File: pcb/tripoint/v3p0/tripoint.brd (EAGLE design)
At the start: 30.5 x 16.4 mm, 72 parts, among them J2 TC2030-JLINK-NL, T1 HHM1595A1, U1 STM32F091CC, U2 DW1000, U3 SKY13317, U4 LXDC2HN18A, X1 38.4M, X2 16M

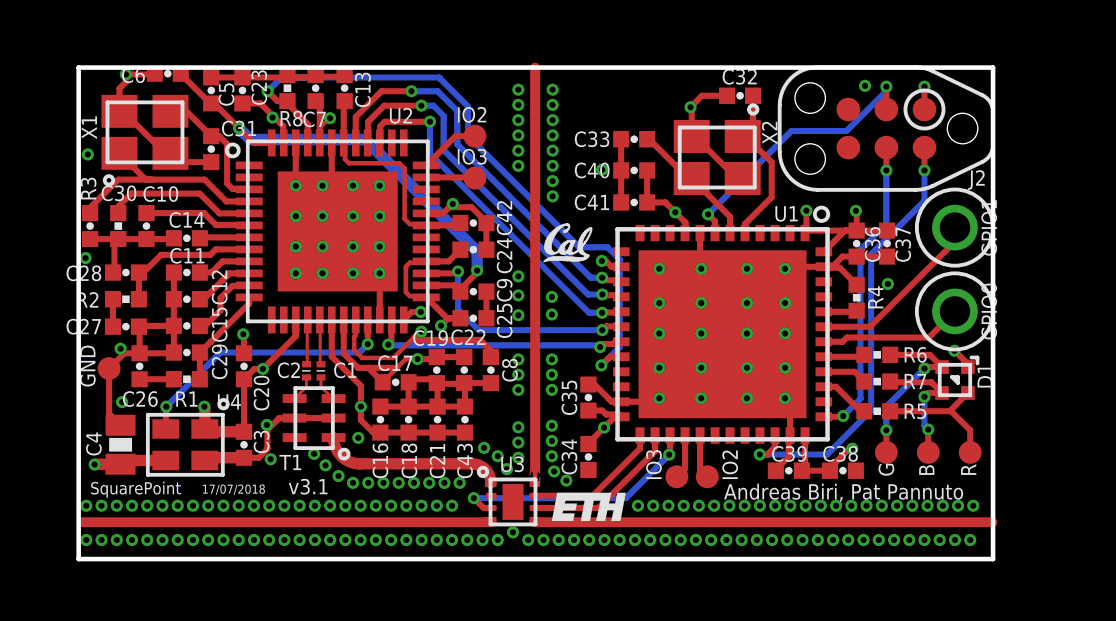
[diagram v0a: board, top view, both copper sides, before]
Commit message: fixed silk screen, increased space between 0201 capacitors
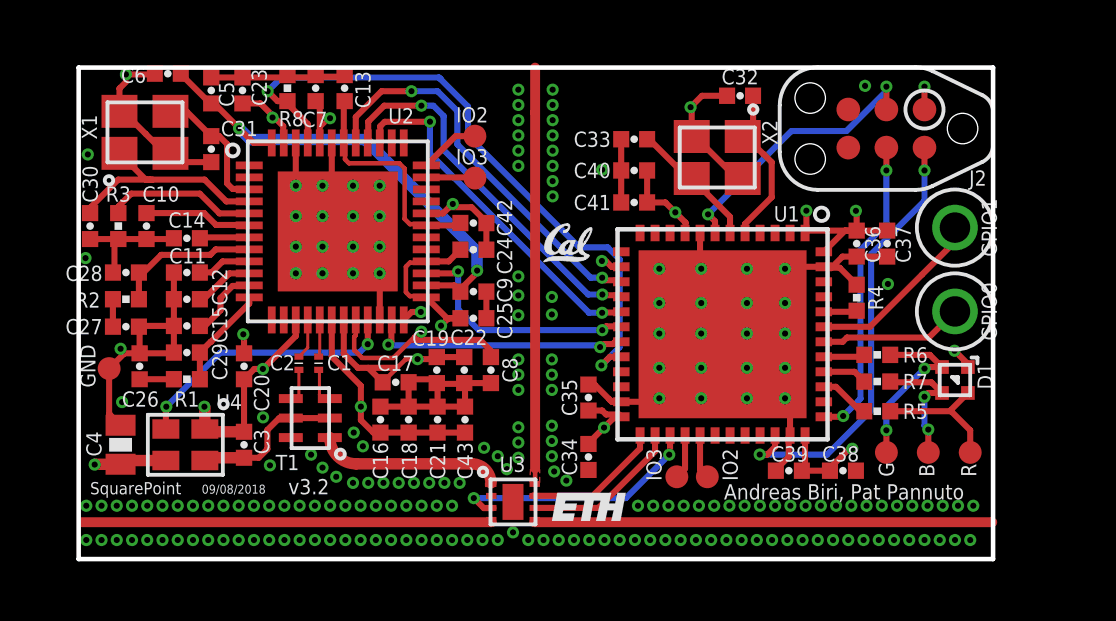
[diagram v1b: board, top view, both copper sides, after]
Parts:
- moved C2 0.36 mm to (-7.90, 0.69)
- moved C1 0.27 mm to (-7.24, 0.69)
- moved T1 0.13 mm to (-7.52, -1.14)
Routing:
- net GND: track 84.2 -> 84.1 mm, vias 204 -> 205
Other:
- board text added: "09/08/2018"
- board text added: "v3.2"
- board text removed: "17/07/2018"
- board text removed: "v3.1"

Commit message: improved RF traces for 0201 capacitors
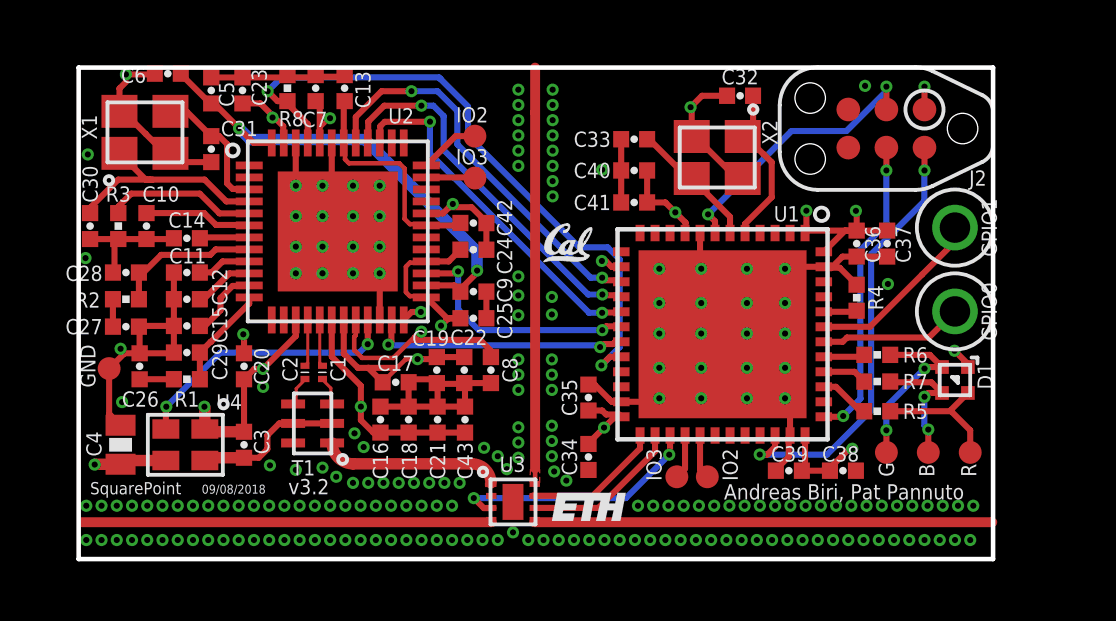
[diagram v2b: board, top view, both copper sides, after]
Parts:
- moved C2 0.37 mm to (-7.70, 0.38)
- moved C1 0.33 mm to (-7.11, 0.38)
- moved T1 0.19 mm to (-7.44, -1.32)
